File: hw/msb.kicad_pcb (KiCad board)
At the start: 2 copper layers, 100 x 90 mm, 95 parts, among them J101 AMPSEAL_8_POS_1-776276-1, J102 AMPSEAL_23_POS_1-776228-1, J302 ARM_JTAG_SWD_HEADER_10_PINSMD, U1001 MOSFET_DRIVER_LT1161, U1002 MOSFET_IPG20N04S4L11ATMA1, U1003 MOSFET_IPG20N04S4L11ATMA1, U1101 ZXCT1086, U1201 ZXCT1086, U1301 ZXCT1086, U1401 ZXCT1086, U1501 ZXCT1086, U1601 ZXCT1086, U301 MCP2551_SOIC8, U302 LPC1549JBD64, U501 MOSFET_DRIVER_LT1161, U502 MOSFET_IPG20N04S4L11ATMA1, U503 MOSFET_IPG20N04S4L11ATMA1, U601 ZXCT1086, U701 ZXCT1086, U801 ZXCT1086, U901 ZXCT1086, X301 XTAL_7A-12.000MAAJ-T

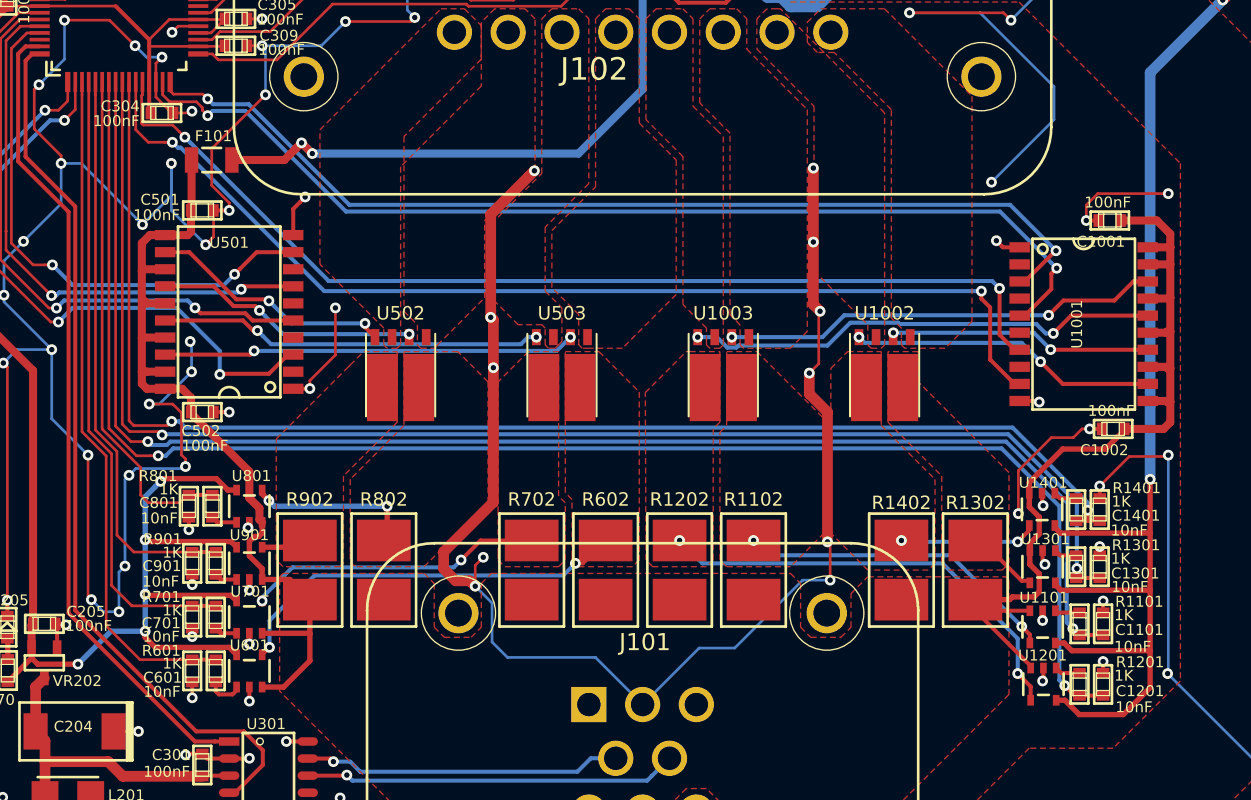
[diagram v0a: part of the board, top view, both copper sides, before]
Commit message: added 1k pull down resistors to mosfet gates
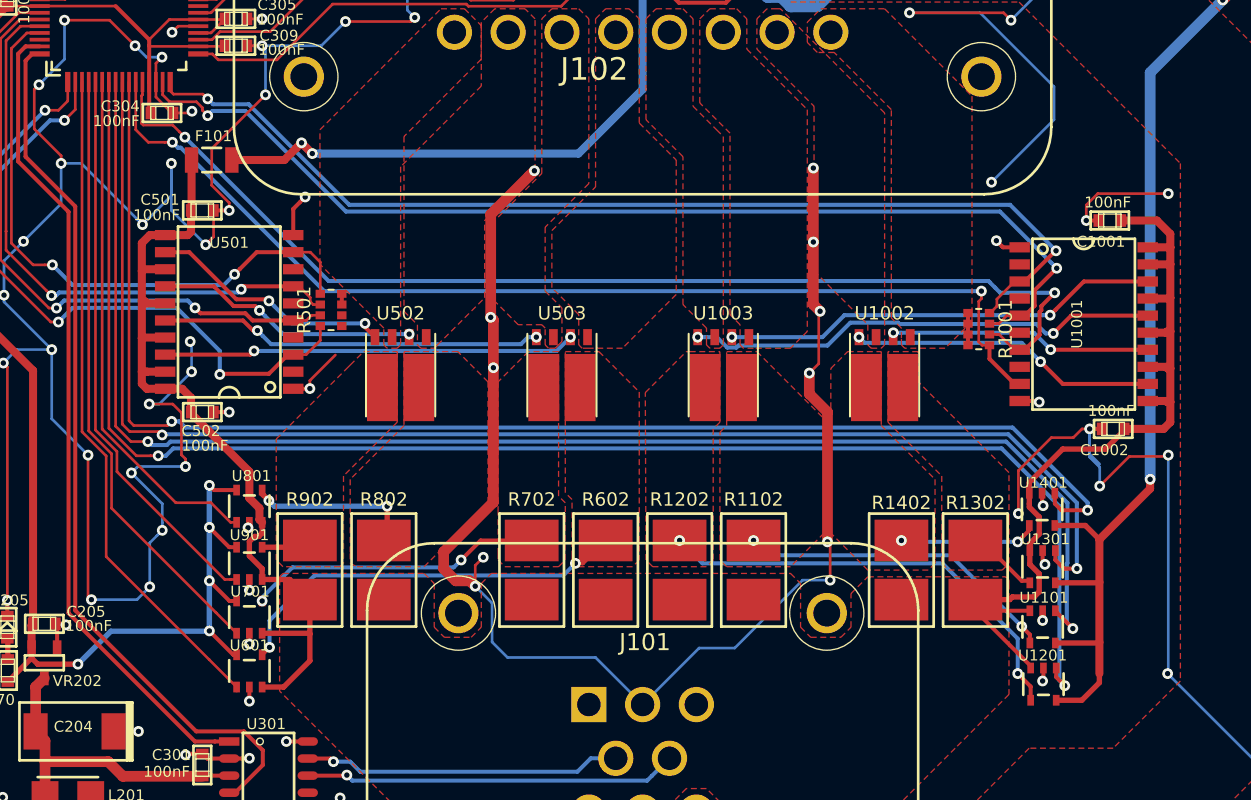
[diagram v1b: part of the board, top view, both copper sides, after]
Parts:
- removed C1101, C1201, C1301, C1401, C601, C701, C801, C901: 10nF, kemet:0603
- removed R1101, R1201, R1301, R1401, R601, R701, R801, R901: 1K, multicomp:0603
- added R1001: R_ARRAY4_1K, usevolt:0603_array4, F.Cu at (193.0, 91.1)
- added R501: R_ARRAY4_1K, usevolt:0603_array4, F.Cu at (144.8, 89.7)
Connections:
- U1101 pad 1: Net-(R1101-Pad1) -> /lpc1549/MOTOR_START_SENSE
- U1201 pad 1: Net-(R1201-Pad1) -> /lpc1549/MOTOR_ON_SENSE
- U1301 pad 1: Net-(R1301-Pad1) -> /lpc1549/ALT_IG_SENSE
- U1401 pad 1: Net-(R1401-Pad1) -> /lpc1549/PUMP_SENSE
- U601 pad 1: Net-(R601-Pad1) -> /lpc1549/GLOW_PLUGS1_SENSE
- U701 pad 1: Net-(R701-Pad1) -> /LT1161/SENSE2
- U801 pad 1: Net-(R801-Pad1) -> /lpc1549/GLOW_PLUGS2_SENSE
- U901 pad 1: Net-(R901-Pad1) -> /lpc1549/CRANE_LIGHT_SENSE
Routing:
- net +3V3: track 370.6 -> 341.9 mm
- net /lpc1549/ALT_IG: track 77.4 -> 84.5 mm
- net /lpc1549/CRANE_LIGHT: track 40.3 -> 45.0 mm
- net /LT1161_2/IN1: track 75.1 -> 78.7 mm
- net /lpc1549/GLOW_PLUGS1: track 49.1 -> 52.7 mm
- net /lpc1549/GLOW_PLUGS2: track 41.6 -> 44.3 mm
- net Net-(R601-Pad1): track 2.70 -> 0.00 mm
- net /LT1161_2/IN2: track 78.1 -> 80.6 mm
- net /LT1161/IN2: track 44.0 -> 46.2 mm
- net Net-(R801-Pad1): track 1.95 -> 0.00 mm
- net Net-(R1201-Pad1): track 1.89 -> 0.00 mm
- net GND: track 728.5 -> 730.4 mm, vias 128 -> 120
- net Net-(R1101-Pad1): track 1.85 -> 0.00 mm
- net Net-(R1401-Pad1): track 1.74 -> 0.00 mm
- net Net-(R901-Pad1): track 1.70 -> 0.00 mm
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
